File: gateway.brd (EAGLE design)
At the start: 100 x 146 mm, 68 parts, among them J1 RASPBERRYPI-40-PIN-GPIO_PTH_N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, Q1 BSS123

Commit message: added reset for IMU
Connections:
- net GPIO5: now also U$4.RST
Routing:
- net GPIO5: track 4.13 -> 35.0 mm
- net RPI_SCL: track 127.8 -> 143.0 mm
- net +3V3: track 15.0 -> 0.00 mm
- net GND: track 232.2 -> 234.0 mm
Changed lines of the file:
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@@
 <wire x1="17.5" y1="99" x2="17.5" y2="102.794" width="1.016" layer="16"/>
 <wire x1="17.5" y1="102.794" x2="17.71" y2="103.004" width="1.016" layer="16"/>
-<wire x1="11.95" y1="92" x2="14" y2="92" width="1.016" layer="1"/>
-<wire x1="14" y1="92" x2="18" y2="96" width="1.016" layer="1"/>
-<wire x1="18" y1="96" x2="18" y2="102.714" width="1.016" layer="1"/>
-<wire x1="18" y1="102.714" x2="17.71" y2="103.004" width="1.016" layer="1"/>
-<wire x1="12.826" y1="127.159" x2="12.826" y2="123.674" width="1.016" layer="1"/>
-<wire x1="12.826" y1="123.674" x2="18" y2="118.5" width="1.016" layer="1"/>
-<wire x1="18" y1="106.5" x2="18" y2="103.294" width="1.016" layer="1"/>
-<wire x1="18" y1="103.294" x2="17.71" y2="103.004" width="1.016" layer="1"/>
 <wire x1="42.54" y1="119" x2="42.54" y2="116.5" width="1.016" layer="1"/>
 <wire x1="42.54" y1="116.5" x2="42.54" y2="114" width="1.016" layer="1"/>
 <wire x1="42.54" y1="114" x2="42.54" y2="111.5" width="1.016" layer="1"/>
-<wire x1="42.5" y1="106" x2="42.5" y2="111.46" width="1.016" layer="1"/>
 <wire x1="42.5" y1="111.46" x2="42.54" y2="111.5" width="1.016" layer="1"/>
-<wire x1="18" y1="118.5" x2="18" y2="106.5" width="1.016" layer="1"/>
-<wire x1="18" y1="106.5" x2="18.5" y2="106" width="1.016" layer="1"/>
-<wire x1="18.5" y1="106" x2="42.5" y2="106" width="1.016" layer="1"/>
-<wire x1="46.27" y1="102.935" x2="45.565" y2="102.935" width="1.016" layer="1"/>
-<wire x1="45.565" y1="102.935" x2="42.5" y2="106" width="1.016" layer="1"/>
 <wire x1="59.5" y1="96" x2="75" y2="96" width="1.016" layer="16"/>
 <wire x1="75" y1="96" x2="79" y2="100" width="1.016" layer="16"/>
 <wire x1="79" y1="100" x2="82.92" y2="100" width="1.016" layer="16"/>
 <wire x1="82.92" y1="100" x2="83" y2="100.08" width="1.016" layer="16"/>
+<wire x1="17.5" y1="103.214" x2="17.71" y2="103.004" width="1.016" layer="16"/>
+<wire x1="42.5" y1="111.46" x2="42.5" y2="106.5" width="1.016" layer="1"/>
+<wire x1="42.5" y1="106.5" x2="42.5" y2="104.935" width="1.016" layer="1"/>
+<wire x1="42.5" y1="104.935" x2="44.5" y2="102.935" width="1.016" layer="1"/>
+<wire x1="44.5" y1="102.935" x2="46.27" y2="102.935" width="1.016" layer="1"/>
+<wire x1="12.826" y1="127.159" x2="12.826" y2="124.174" width="1.016" layer="1"/>
+<wire x1="12.826" y1="124.174" x2="17.5" y2="119.5" width="1.016" layer="1"/>
+<wire x1="17.5" y1="119.5" x2="17.5" y2="103.214" width="1.016" layer="1"/>
+<wire x1="17.5" y1="103.214" x2="17.71" y2="103.004" width="1.016" layer="1"/>
+<wire x1="17.71" y1="103.004" x2="17.71" y2="97.76" width="1.016" layer="1"/>
+<wire x1="17.71" y1="97.76" x2="11.95" y2="92" width="1.016" layer="1"/>
+<wire x1="17.71" y1="103.004" x2="17.71" y2="104.71" width="1.016" layer="1"/>
+<wire x1="17.71" y1="104.71" x2="19.5" y2="106.5" width="1.016" layer="1"/>
+<wire x1="19.5" y1="106.5" x2="42.5" y2="106.5" width="1.016" layer="1"/>
 <wire x1="82.58" y1="100.08" x2="80.58" y2="138.26" width="0" layer="19" extent="16-16"/>
 <wire x1="7.04" y1="56.17" x2="7" y2="71" width="0" layer="19" extent="1-1"/>
@@
 <signal name="+3V3">
 <contactref element="J1" pad="1"/>
-<wire x1="75.92" y1="89.92" x2="70" y2="84" width="0.8128" layer="1"/>
-<wire x1="70" y1="84" x2="70" y2="77.62" width="0.8128" layer="1"/>
-<wire x1="70" y1="77.62" x2="69.85" y2="77.47" width="0.8128" layer="1"/>
 </signal>
 <signal name="RPI_SDA">
@@
 <contactref element="U$4" pad="SCL"/>
 <contactref element="MS1" pad="18"/>
-<wire x1="46.27" y1="97.855" x2="48.5" y2="97.855" width="1.016" layer="1"/>
-<wire x1="48.5" y1="97.855" x2="51.355" y2="97.855" width="1.016" layer="1"/>
-<wire x1="51.355" y1="97.855" x2="53" y2="99.5" width="1.016" layer="1"/>
-<wire x1="83" y1="95" x2="64" y2="95" width="1.016" layer="1"/>
-<wire x1="59.5" y1="99.5" x2="53" y2="99.5" width="1.016" layer="1"/>
 <wire x1="43" y1="96.5" x2="23" y2="96.5" width="1.016" layer="16"/>
 <wire x1="23" y1="96.5" x2="20" y2="99.5" width="1.016" layer="16"/>
 <wire x1="20" y1="99.5" x2="20" y2="102.754" width="1.016" layer="16"/>
 <wire x1="20" y1="102.754" x2="20.25" y2="103.004" width="1.016" layer="16"/>
-<wire x1="53" y1="99.5" x2="53" y2="117.58" width="1.016" layer="1"/>
-<wire x1="53" y1="117.58" x2="52.64" y2="117.94" width="1.016" layer="1"/>
-<wire x1="59.5" y1="99.5" x2="64" y2="95" width="1.016" layer="1"/>
 <wire x1="46.27" y1="97.855" x2="44.355" y2="97.855" width="1.016" layer="16"/>
 <wire x1="44.355" y1="97.855" x2="43" y2="96.5" width="1.016" layer="16"/>
-<wire x1="69.85" y1="72.39" x2="63.11" y2="72.39" width="1.016" layer="1"/>
-<wire x1="63.11" y1="72.39" x2="58.5" y2="77" width="1.016" layer="1"/>
-<wire x1="58.5" y1="77" x2="58.5" y2="87.855" width="1.016" layer="1"/>
-<wire x1="58.5" y1="87.855" x2="48.5" y2="97.855" width="1.016" layer="1"/>
+<wire x1="46.27" y1="97.855" x2="50.645" y2="97.855" width="1.016" layer="16"/>
+<wire x1="50.645" y1="97.855" x2="59" y2="89.5" width="1.016" layer="16"/>
+<wire x1="59" y1="89.5" x2="59" y2="74" width="1.016" layer="16"/>
+<wire x1="59" y1="74" x2="60.5" y2="72.5" width="1.016" layer="16"/>
+<wire x1="60.5" y1="72.5" x2="69.74" y2="72.5" width="1.016" layer="16"/>
+<wire x1="69.74" y1="72.5" x2="69.85" y2="72.39" width="1.016" layer="16"/>
+<wire x1="83" y1="95" x2="72.5" y2="95" width="1.016" layer="1"/>
+<wire x1="72.5" y1="95" x2="64" y2="86.5" width="1.016" layer="1"/>
+<wire x1="64" y1="86.5" x2="64" y2="73" width="1.016" layer="1"/>
+<wire x1="64" y1="73" x2="64.5" y2="72.5" width="1.016" layer="1"/>
+<wire x1="64.5" y1="72.5" x2="69.74" y2="72.5" width="1.016" layer="1"/>
+<wire x1="69.74" y1="72.5" x2="69.85" y2="72.39" width="1.016" layer="1"/>
+<wire x1="52.64" y1="117.94" x2="52.64" y2="99.14" width="1.016" layer="1"/>
+<wire x1="52.64" y1="99.14" x2="51" y2="97.5" width="1.016" layer="1"/>
+<wire x1="51" y1="97.5" x2="46.625" y2="97.5" width="1.016" layer="1"/>
+<wire x1="46.625" y1="97.5" x2="46.27" y2="97.855" width="1.016" layer="1"/>
 </signal>
 <signal name="N$4">
@@
 </polygon>
 <contactref element="FUSE1" pad="1"/>
-<wire x1="22" y1="47.55" x2="28" y2="47.55" width="0" layer="19" extent="1-1"/>
-<wire x1="22" y1="42" x2="22" y2="47.55" width="0" layer="19" extent="1-1"/>
-<wire x1="28.075" y1="33.0475" x2="22" y2="42" width="0" layer="19" extent="1-1"/>
 </signal>
 <signal name="BATT-">
@@
 </polygon>
 <wire x1="7" y1="46.5936" x2="7" y2="45.5" width="0.6096" layer="1"/>
-<wire x1="7" y1="46.5936" x2="11.5" y2="49.9" width="0" layer="19" extent="1-1"/>
-<wire x1="7" y1="42" x2="7" y2="45.5" width="0" layer="19" extent="1-1"/>
-<wire x1="26.075" y1="33.0475" x2="7" y2="42" width="0" layer="19" extent="1-1"/>
 </signal>
 <signal name="RPI_GPIO18">
@@
 <wire x1="6.5" y1="125.5" x2="6.5" y2="81.4425" width="1.27" layer="16"/>
 <wire x1="6.5" y1="81.4425" x2="8.0275" y2="79.915" width="1.27" layer="16"/>
-<wire x1="10.286" y1="127.159" x2="14.5936" y2="133.5" width="0" layer="19" extent="1-1"/>
 </signal>
 <signal name="INA_VIN-">
@@
 <vertex x="13.5" y="51.5"/>
 </polygon>
-<wire x1="12.45" y1="52.1" x2="16.44" y2="56.17" width="0" layer="19" extent="1-1"/>
 <wire x1="25.33" y1="103.004" x2="25.33" y2="89.83" width="1.016" layer="1"/>
 <wire x1="25.33" y1="89.83" x2="20" y2="84.5" width="1.016" layer="1"/>
 <wire x1="20" y1="84.5" x2="20" y2="80.5" width="1.016" layer="1"/>
-<wire x1="20" y1="80.5" x2="16.44" y2="56.17" width="0" layer="19" extent="1-16"/>
 </signal>
 <signal name="INA_VIN+">
@@
 </polygon>
 <contactref element="FUSE1" pad="2"/>
-<wire x1="22" y1="52.45" x2="28" y2="52.45" width="0" layer="19" extent="1-1"/>
 <wire x1="27.87" y1="103.004" x2="27.87" y2="79.37" width="1.016" layer="1"/>
 <wire x1="27.87" y1="79.37" x2="27.5" y2="79" width="1.016" layer="1"/>
-<wire x1="27.5" y1="79" x2="28" y2="52.45" width="0" layer="19" extent="1-16"/>
 </signal>
 <signal name="3.3V">
@@
 <vertex x="10.5" y="27"/>
 </polygon>
-<wire x1="7" y1="19" x2="26.075" y2="20.0475" width="0" layer="19" extent="1-1"/>
 </signal>
 <signal name="DELAY">
@@
 <vertex x="18.5" y="134"/>
 </polygon>
-<wire x1="15.4064" y1="133.5" x2="17.906" y2="127.159" width="0" layer="19" extent="1-1"/>
 <wire x1="72.96" y1="117.94" x2="72.96" y2="126.54" width="1.27" layer="1"/>
 <wire x1="72.96" y1="126.54" x2="72" y2="127.5" width="1.27" layer="1"/>
@@
 <vertex x="30" y="27"/>
 </polygon>
-<wire x1="22" y1="19" x2="28.075" y2="20.0475" width="0" layer="19" extent="1-1"/>
 </signal>
 <signal name="N$2">
@@
 <wire x1="55.18" y1="117.94" x2="55.18" y2="121.82" width="1.016" layer="1"/>
 <wire x1="55.18" y1="121.82" x2="55" y2="122" width="1.016" layer="1"/>
+<contactref element="U$4" pad="RST"/>
+<wire x1="55.18" y1="117.94" x2="55.18" y2="97.68" width="1.016" layer="1"/>
+<wire x1="55.18" y1="97.68" x2="52" y2="94.5" width="1.016" layer="1"/>
+<wire x1="52" y1="94.5" x2="47.085" y2="94.5" width="1.016" layer="1"/>
+<wire x1="47.085" y1="94.5" x2="46.27" y2="95.315" width="1.016" layer="1"/>
 </signal>
 <signal name="N$1">

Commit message: added header for main_switch
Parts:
- added MAIN_SWITCH: JST-PH_2-PIN_HEADER, SRG:JST_B2B-PH_HEADER
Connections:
- new net N$13: BATT.P1, MAIN_SWITCH.P1
- net BATT+: now also MAIN_SWITCH.P2; no longer BATT.P1
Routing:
- net BATT+: track 0.00 -> 9.64 mm
- net N$13: track 0.00 -> 9.00 mm
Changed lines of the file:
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@@
 <attribute name="NAME" x="35.25" y="24" size="0.8128" layer="25" rot="R180"/>
 </element>
+<element name="MAIN_SWITCH" library="SRG" package="JST_B2B-PH_HEADER" value="JST-PH_2-PIN_HEADER" x="27" y="42"/>
 </elements>
 <signals>
@@
 <wire x1="17.71" y1="104.71" x2="19.5" y2="106.5" width="1.016" layer="1"/>
 <wire x1="19.5" y1="106.5" x2="42.5" y2="106.5" width="1.016" layer="1"/>
-<wire x1="82.58" y1="100.08" x2="80.58" y2="138.26" width="0" layer="19" extent="16-16"/>
-<wire x1="7.04" y1="56.17" x2="7" y2="71" width="0" layer="19" extent="1-1"/>
-<wire x1="10.55" y1="52.1" x2="7.04" y2="56.17" width="0" layer="19" extent="1-1"/>
-<wire x1="7" y1="47.5" x2="10.5" y2="52" width="0" layer="19" extent="1-1"/>
-<wire x1="72.39" y1="72.39" x2="75" y2="96" width="0" layer="19" extent="16-16"/>
-<wire x1="69.85" y1="67.31" x2="72.39" y2="72.39" width="0" layer="19" extent="1-1"/>
-<wire x1="72.39" y1="62.23" x2="69.85" y2="67.31" width="0" layer="19" extent="1-1"/>
-<wire x1="72.39" y1="54.61" x2="72.39" y2="62.23" width="0" layer="19" extent="1-1"/>
-<wire x1="69.85" y1="46.99" x2="72.39" y2="54.61" width="0" layer="19" extent="1-1"/>
-<wire x1="69.85" y1="41.91" x2="69.85" y2="46.99" width="0" layer="19" extent="1-1"/>
-<wire x1="72.39" y1="41.91" x2="69.85" y2="41.91" width="0" layer="19" extent="1-1"/>
-<wire x1="72.39" y1="39.37" x2="72.39" y2="41.91" width="0" layer="19" extent="1-1"/>
-<wire x1="72.39" y1="36.83" x2="72.39" y2="39.37" width="0" layer="19" extent="1-1"/>
-<wire x1="72.39" y1="34.29" x2="72.39" y2="36.83" width="0" layer="19" extent="1-1"/>
-<wire x1="69.85" y1="29.21" x2="72.39" y2="34.29" width="0" layer="19" extent="1-1"/>
 </signal>
 <signal name="RPI_TX">
@@
 <signal name="BATT+">
 <contactref element="U$1" pad="VOUT+"/>
-<contactref element="BATT" pad="P1"/>
 <contactref element="FUSE" pad="1"/>
 <polygon width="0.6096" layer="1" thermals="no">
 <vertex x="19.5" y="49"/>
-<vertex x="19.5" y="41"/>
-<vertex x="28" y="41"/>
-<vertex x="28" y="30"/>
-<vertex x="30" y="30"/>
+<vertex x="19.5" y="45.5"/>
+<vertex x="30" y="45.5"/>
 <vertex x="30" y="49"/>
 </polygon>
 <contactref element="FUSE1" pad="1"/>
+<contactref element="MAIN_SWITCH" pad="P2"/>
+<wire x1="26.075" y1="42.0475" x2="22.0475" y2="42.0475" width="1.27" layer="1"/>
+<wire x1="22.0475" y1="42.0475" x2="22" y2="42" width="1.27" layer="1"/>
+<wire x1="22" y1="42" x2="22" y2="47.55" width="1.27" layer="1"/>
 </signal>
 <signal name="BATT-">
@@
 <wire x1="15.5" y1="72.51" x2="16.44" y2="71.57" width="1.27" layer="1"/>
 </signal>
+<signal name="N$13">
+<contactref element="BATT" pad="P1"/>
+<contactref element="MAIN_SWITCH" pad="P1"/>
+<wire x1="28.075" y1="33.0475" x2="28.075" y2="42.0475" width="1.27" layer="1"/>
+</signal>
 </signals>

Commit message: added soms
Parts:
- added PAD41: WIREPADSMD1,27-254, wirepad:SMD1,27-2,54
- added SOMS: B3B-ZR, jst:B3B-ZR
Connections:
- new net N$15: PAD41.1, SOMS.2
- net FEATHER_3.3V: now also SOMS.3
- net GND: now also SOMS.1
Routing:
- net GND: track 234.0 -> 253.0 mm
- net FEATHER_3.3V: track 267.1 -> 286.1 mm
- net N$15: track 0.00 -> 5.00 mm
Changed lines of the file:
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@@
 </element>
 <element name="MAIN_SWITCH" library="SRG" package="JST_B2B-PH_HEADER" value="JST-PH_2-PIN_HEADER" x="27" y="42"/>
+<element name="SOMS" library="jst" package="B3B-ZR" value="B3B-ZR" x="35" y="39.5" smashed="yes" rot="R180">
+<attribute name="NAME" x="38.75" y="38" size="1.27" layer="25" rot="R180"/>
+</element>
+<element name="PAD41" library="wirepad" package="SMD1,27-2,54" value="WIREPADSMD1,27-254" x="35" y="34.5" smashed="yes"/>
 </elements>
 <signals>
@@
 <wire x1="17.71" y1="104.71" x2="19.5" y2="106.5" width="1.016" layer="1"/>
 <wire x1="19.5" y1="106.5" x2="42.5" y2="106.5" width="1.016" layer="1"/>
+<contactref element="SOMS" pad="1"/>
+<wire x1="36.5" y1="39.5" x2="36.5" y2="20.5" width="1.016" layer="16"/>
+<wire x1="82.58" y1="100.08" x2="80.58" y2="138.26" width="0" layer="19" extent="16-16"/>
+<wire x1="7.04" y1="56.17" x2="7" y2="71" width="0" layer="19" extent="1-1"/>
+<wire x1="10.55" y1="52.1" x2="7.04" y2="56.17" width="0" layer="19" extent="1-1"/>
+<wire x1="7" y1="47.5" x2="10.5" y2="52" width="0" layer="19" extent="1-1"/>
+<wire x1="72.39" y1="72.39" x2="75" y2="96" width="0" layer="19" extent="16-16"/>
+<wire x1="69.85" y1="67.31" x2="72.39" y2="72.39" width="0" layer="19" extent="1-1"/>
+<wire x1="72.39" y1="62.23" x2="69.85" y2="67.31" width="0" layer="19" extent="1-1"/>
+<wire x1="72.39" y1="54.61" x2="72.39" y2="62.23" width="0" layer="19" extent="1-1"/>
+<wire x1="69.85" y1="46.99" x2="72.39" y2="54.61" width="0" layer="19" extent="1-1"/>
+<wire x1="69.85" y1="41.91" x2="69.85" y2="46.99" width="0" layer="19" extent="1-1"/>
+<wire x1="72.39" y1="41.91" x2="69.85" y2="41.91" width="0" layer="19" extent="1-1"/>
+<wire x1="72.39" y1="39.37" x2="72.39" y2="41.91" width="0" layer="19" extent="1-1"/>
+<wire x1="72.39" y1="36.83" x2="72.39" y2="39.37" width="0" layer="19" extent="1-1"/>
+<wire x1="72.39" y1="34.29" x2="72.39" y2="36.83" width="0" layer="19" extent="1-1"/>
+<wire x1="69.85" y1="29.21" x2="72.39" y2="34.29" width="0" layer="19" extent="1-1"/>
 </signal>
 <signal name="RPI_TX">
@@
 <contactref element="RAIN" pad="3"/>
 <wire x1="88" y1="89" x2="88" y2="112" width="1.016" layer="16"/>
-<wire x1="33.5" y1="20.5" x2="32.5" y2="19.5" width="1.016" layer="16"/>
-<wire x1="32.5" y1="19.5" x2="32.5" y2="15.5" width="1.016" layer="16"/>
 <wire x1="32.5" y1="15.5" x2="33.5" y2="14.5" width="1.016" layer="16"/>
 <wire x1="15.17" y1="103.004" x2="15.17" y2="104.67" width="1.016" layer="16"/>
@@
 <wire x1="46.27" y1="108.015" x2="61.015" y2="108.015" width="1.016" layer="16"/>
 <wire x1="61.015" y1="108.015" x2="62.5" y2="109.5" width="1.016" layer="16"/>
+<contactref element="SOMS" pad="3"/>
+<wire x1="32.5" y1="15.5" x2="32.5" y2="19.5" width="1.016" layer="16"/>
+<wire x1="32.5" y1="19.5" x2="33.5" y2="20.5" width="1.016" layer="16"/>
+<wire x1="33.5" y1="20.5" x2="33.5" y2="39.5" width="1.016" layer="16"/>
 </signal>
 <signal name="EN">
@@
 <wire x1="28.075" y1="33.0475" x2="28.075" y2="42.0475" width="1.27" layer="1"/>
 </signal>
+<signal name="N$15">
+<contactref element="SOMS" pad="2"/>
+<contactref element="PAD41" pad="1"/>
+<wire x1="35" y1="39.5" x2="35" y2="34.5" width="1.016" layer="1"/>
+</signal>
 </signals>

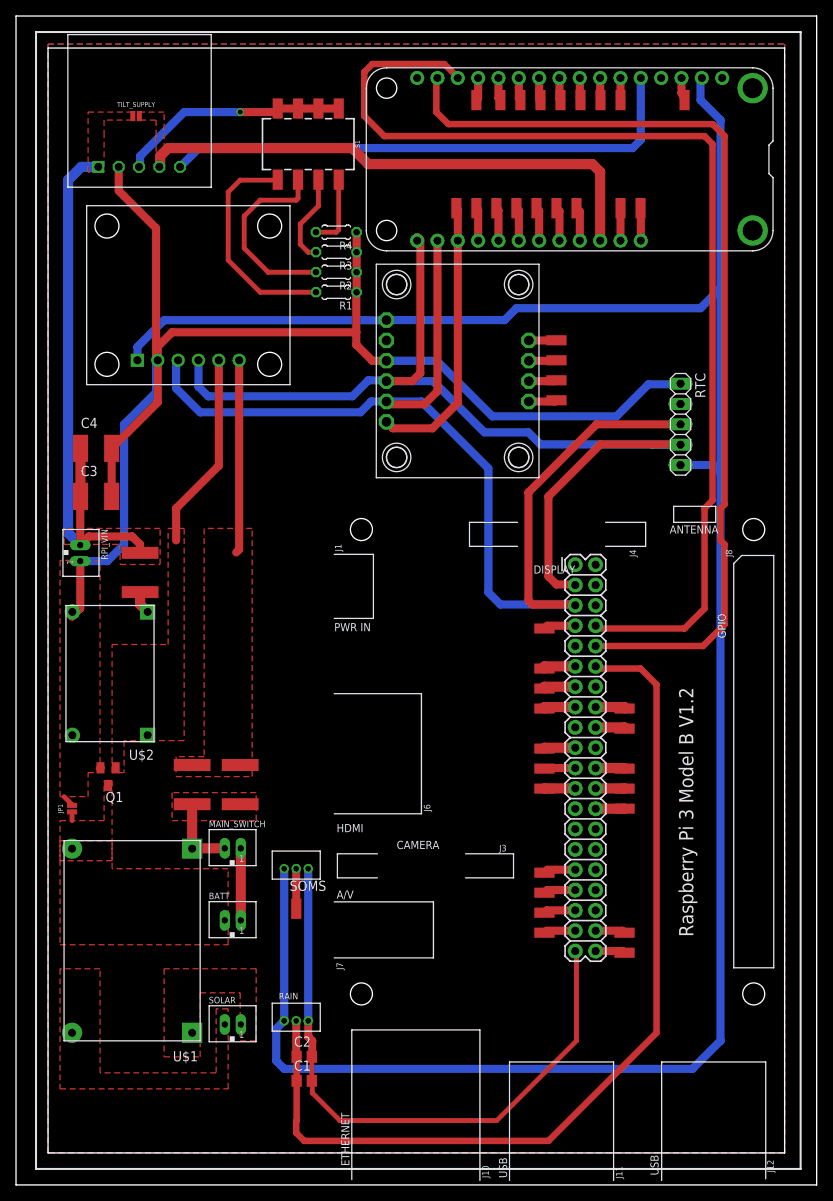
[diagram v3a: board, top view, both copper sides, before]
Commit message: Added a v2 for the tilt_soms_lgbu board (tilt_soms_lgbu_v2)
Primary changes:
Placed all components on top layer including the con-wago connectors.
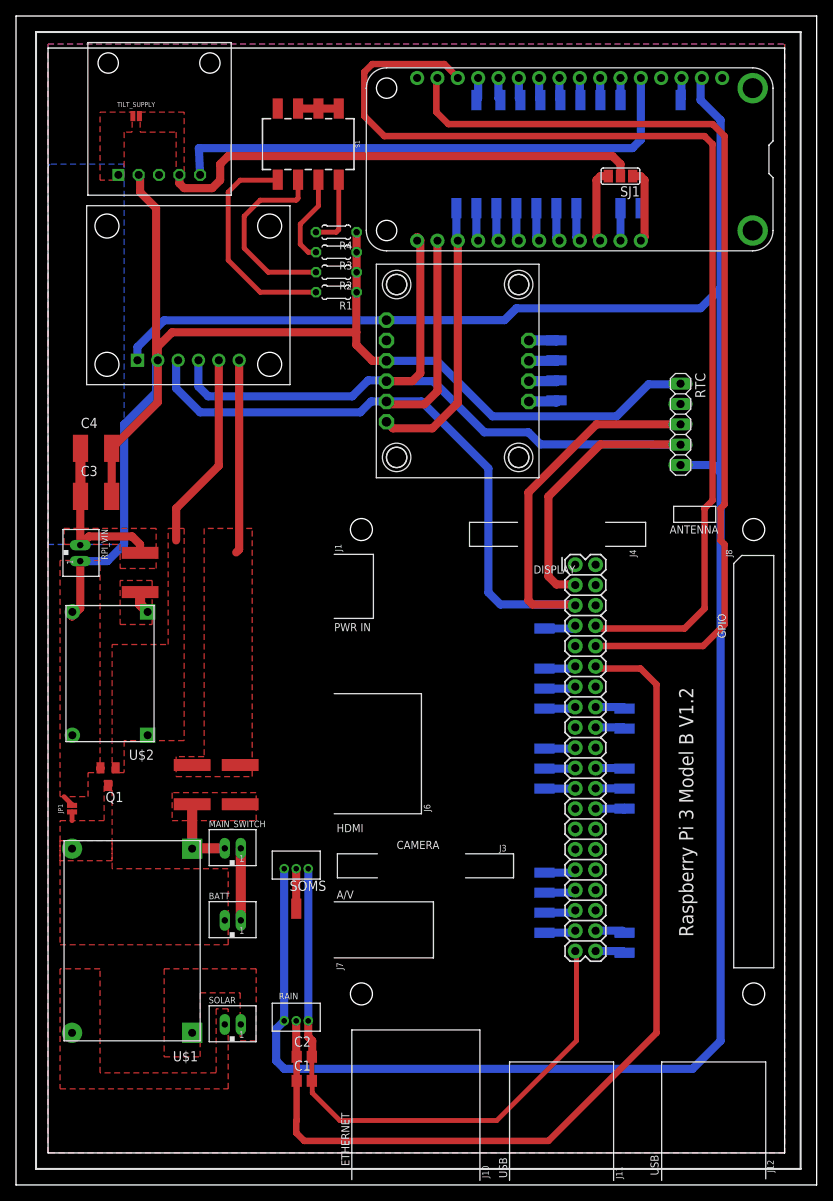
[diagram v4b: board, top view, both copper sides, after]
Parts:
- added SJ1: (no value), jumper:SJ_2
- moved U$3 2.69 mm to (10.5, 124.0)
- moved PAD13 0.50 mm to (83.0, 135.5), flipped to the bottom
- flipped PAD1 to the bottom
- flipped PAD10 to the bottom
- flipped PAD11 to the bottom
- flipped PAD12 to the bottom
- flipped PAD14 to the bottom
- flipped PAD15 to the bottom
- flipped PAD16 to the bottom
- flipped PAD17 to the bottom
- flipped PAD18 to the bottom
- flipped PAD19 to the bottom
- flipped PAD2 to the bottom
- flipped PAD20 to the bottom
- flipped PAD21 to the bottom
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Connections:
- net +5V renamed VOLTAGE_SUPPLY
- new net FEATHER_BAT: MS1.28, SJ1.1
- new net FEATHER_SUPPLY: SJ1.2, TILT_SUPPLY.2, U$3.DRV
- net FEATHER_USB: now also SJ1.3; no longer TILT_SUPPLY.2, U$3.DRV
- net VBAT: no longer MS1.28
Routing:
- net FEATHER_SUPPLY: track 0.00 -> 61.1 mm
- net FEATHER_USB: track 66.6 -> 9.43 mm
- net VOLTAGE_SUPPLY: track 72.2 -> 21.5 mm
- net DELAY: track 29.2 -> 5.08 mm, vias 1 -> 0
- net FEATHER_BAT: track 0.00 -> 9.43 mm
- net VBAT: track 4.08 -> 0.00 mm
- net GND: track 253.0 -> 250.9 mm
- added copper zone on layer 1, net FEATHER_SUPPLY
- added copper zone on layer 1, net N$8
- added copper zone on layer 16, net VOLTAGE_SUPPLY
- removed copper zone on layer 1, net FEATHER_USB
